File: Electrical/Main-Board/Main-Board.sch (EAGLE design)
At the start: 30 parts, among them IC1 ATMEGA16A-PU, IC2 ATMEGA16A-PU, IC3 TLE4966L, IC5 LM2904DRG3, IC6 TLE4966L, J1 FTSH-105-01-L-DV-K-A-P-TR, J2 0022288033, J3 0022288033, J4 PJ-031DH

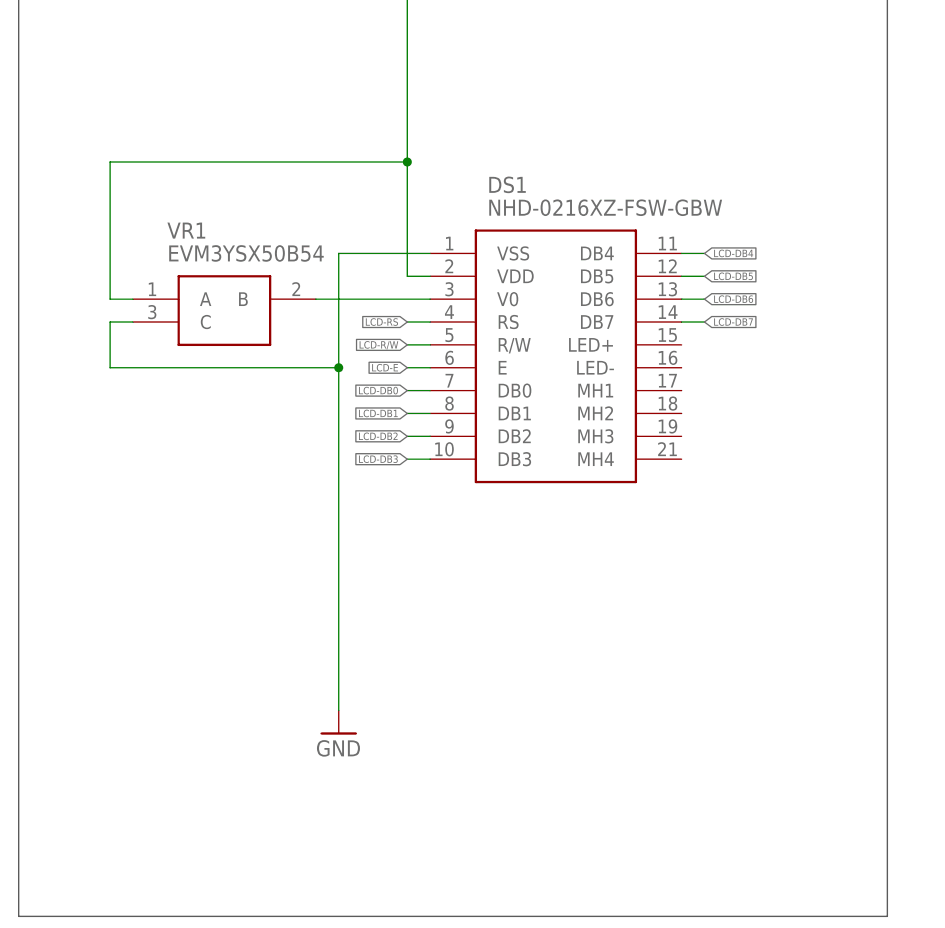
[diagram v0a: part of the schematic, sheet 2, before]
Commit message: Updated display footprint and fixed layout to suit it.
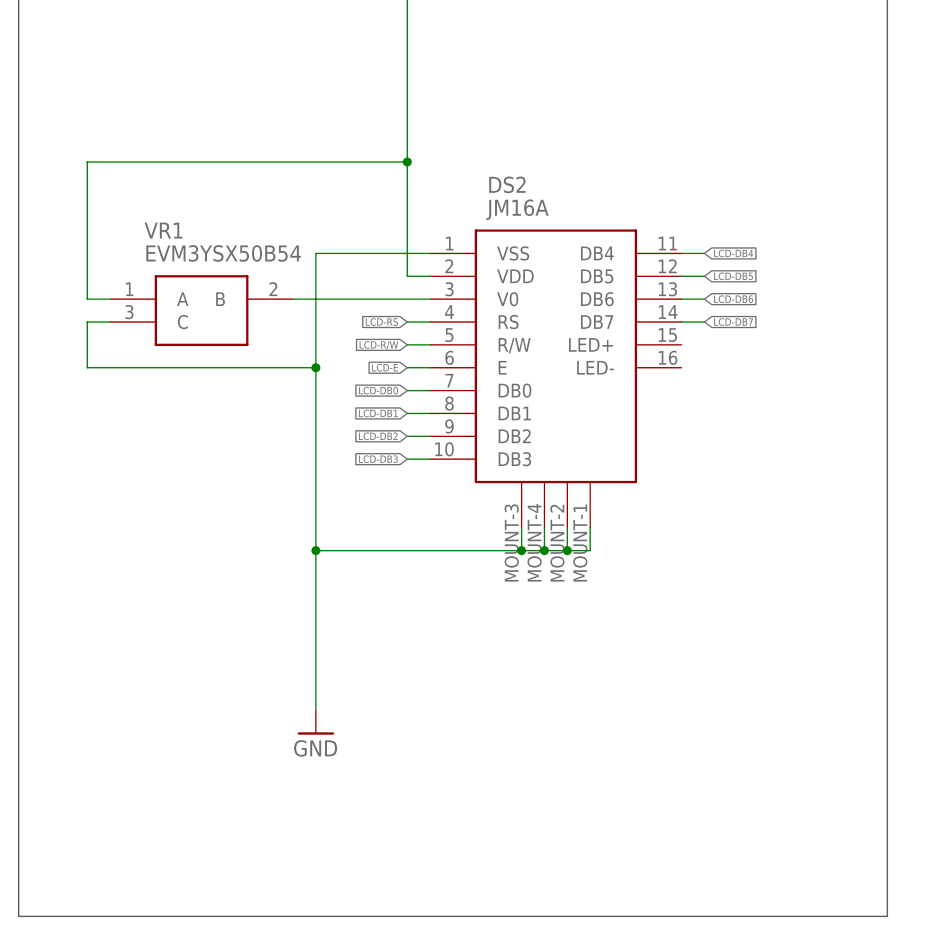
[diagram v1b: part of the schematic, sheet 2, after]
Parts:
- removed DS1: NHD-0216XZ-FSW-GBW, SamacSys_Parts:NHD-0216XZ-FSW-GBW
- added DS2: JM16A, JM16A-Vanheden:JM16A
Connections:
- net +5V/1: now also DS2.VDD; no longer DS1.VDD
- net GND: now also DS2.MOUNT-1, DS2.MOUNT-2, DS2.MOUNT-3, DS2.MOUNT-4, DS2.VSS; no longer DS1.VSS
- net LCD-DB0: now also DS2.DB0; no longer DS1.DB0
- net LCD-DB1: now also DS2.DB1; no longer DS1.DB1
- net LCD-DB2: now also DS2.DB2; no longer DS1.DB2
- net LCD-DB3: now also DS2.DB3; no longer DS1.DB3
- net LCD-DB4: now also DS2.DB4; no longer DS1.DB4
- net LCD-DB5: now also DS2.DB5; no longer DS1.DB5
- net LCD-DB6: now also DS2.DB6; no longer DS1.DB6
- net LCD-DB7: now also DS2.DB7; no longer DS1.DB7
- net LCD-E: now also DS2.E; no longer DS1.E
- net LCD-R/W: now also DS2.R/W; no longer DS1.R/W
- net LCD-RS: now also DS2.RS; no longer DS1.RS
- net N$2: now also DS2.V0; no longer DS1.V0
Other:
- moved on the sheet: VR1
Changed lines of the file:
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@@
 <drawing>
 <settings>
-<setting alwaysvectorfont="no"/>
+<setting alwaysvectorfont="yes"/>
 <setting verticaltext="up"/>
 </settings>
@@
 <part name="S2" library="SamacSys_Parts" deviceset="PTS647SM50SMTR2LFS" device=""/>
 <part name="R4" library="rcl" library_urn="urn:adsk.eagle:library:334" deviceset="R-EU_" device="R0603" package3d_urn="urn:adsk.eagle:package:23555/3" value="10K/10%"/>
-<part name="DS1" library="SamacSys_Parts" deviceset="NHD-0216XZ-FSW-GBW" device=""/>
 <part name="GND6" library="supply1" library_urn="urn:adsk.eagle:library:371" deviceset="GND" device=""/>
 <part name="SUPPLY6" library="supply2" library_urn="urn:adsk.eagle:library:372" deviceset="+5V/1" device=""/>
@@
 <part name="FRAME3" library="frames" library_urn="urn:adsk.eagle:library:229" deviceset="A4L-LOC" device=""/>
 <part name="C7" library="SamacSys_Parts" deviceset="EEEFK1J220P" device=""/>
+<part name="DS2" library="JM16A-Vanheden" deviceset="JM16A" device=""/>
 </parts>
 <sheets>
@@
 <attribute name="SHEET" x="230.505" y="5.08" size="2.54" layer="94"/>
 </instance>
-<instance part="DS1" gate="G$1" x="66.04" y="104.14" smashed="yes">
-<attribute name="NAME" x="72.39" y="111.76" size="1.778" layer="95" align="center-left"/>
-<attribute name="VALUE" x="72.39" y="109.22" size="1.778" layer="96" align="center-left"/>
-</instance>
-<instance part="GND6" gate="1" x="55.88" y="50.8" smashed="yes">
-<attribute name="VALUE" x="53.34" y="48.26" size="1.778" layer="96"/>
+<instance part="GND6" gate="1" x="53.34" y="50.8" smashed="yes">
+<attribute name="VALUE" x="50.8" y="48.26" size="1.778" layer="96"/>
 </instance>
 <instance part="SUPPLY6" gate="G$1" x="63.5" y="137.16" smashed="yes">
 <attribute name="VALUE" x="60.325" y="140.335" size="1.778" layer="96"/>
 </instance>
-<instance part="VR1" gate="G$1" x="33.02" y="99.06" smashed="yes">
-<attribute name="NAME" x="36.83" y="106.68" size="1.778" layer="95" align="center-left"/>
-<attribute name="VALUE" x="36.83" y="104.14" size="1.778" layer="96" align="center-left"/>
+<instance part="VR1" gate="G$1" x="30.48" y="99.06" smashed="yes">
+<attribute name="NAME" x="34.29" y="106.68" size="1.778" layer="95" align="center-left"/>
+<attribute name="VALUE" x="34.29" y="104.14" size="1.778" layer="96" align="center-left"/>
 </instance>
 <instance part="JP1" gate="A" x="187.96" y="91.44" smashed="yes" rot="R180">
@@
 <instance part="SUPPLY9" gate="G$1" x="205.74" y="111.76" smashed="yes">
 <attribute name="VALUE" x="202.565" y="114.935" size="1.778" layer="96"/>
+</instance>
+<instance part="DS2" gate="G$1" x="66.04" y="104.14" smashed="yes">
+<attribute name="NAME" x="72.39" y="111.76" size="1.778" layer="95" align="center-left"/>
+<attribute name="VALUE" x="72.39" y="109.22" size="1.778" layer="96" align="center-left"/>
 </instance>
 </instances>
@@
 <net name="GND" class="0">
 <segment>
-<pinref part="DS1" gate="G$1" pin="VSS"/>
-<wire x1="66.04" y1="104.14" x2="55.88" y2="104.14" width="0.1524" layer="91"/>
-<wire x1="55.88" y1="104.14" x2="55.88" y2="91.44" width="0.1524" layer="91"/>
+<wire x1="66.04" y1="104.14" x2="53.34" y2="104.14" width="0.1524" layer="91"/>
+<wire x1="53.34" y1="104.14" x2="53.34" y2="91.44" width="0.1524" layer="91"/>
 <pinref part="GND6" gate="1" pin="GND"/>
 <pinref part="VR1" gate="G$1" pin="C"/>
-<wire x1="55.88" y1="91.44" x2="55.88" y2="53.34" width="0.1524" layer="91"/>
-<wire x1="33.02" y1="96.52" x2="30.48" y2="96.52" width="0.1524" layer="91"/>
-<wire x1="30.48" y1="96.52" x2="30.48" y2="91.44" width="0.1524" layer="91"/>
-<wire x1="30.48" y1="91.44" x2="55.88" y2="91.44" width="0.1524" layer="91"/>
-<junction x="55.88" y="91.44"/>
+<wire x1="53.34" y1="91.44" x2="53.34" y2="71.12" width="0.1524" layer="91"/>
+<wire x1="53.34" y1="71.12" x2="53.34" y2="53.34" width="0.1524" layer="91"/>
+<wire x1="30.48" y1="96.52" x2="27.94" y2="96.52" width="0.1524" layer="91"/>
+<wire x1="27.94" y1="96.52" x2="27.94" y2="91.44" width="0.1524" layer="91"/>
+<wire x1="27.94" y1="91.44" x2="53.34" y2="91.44" width="0.1524" layer="91"/>
+<junction x="53.34" y="91.44"/>
+<pinref part="DS2" gate="G$1" pin="VSS"/>
+<pinref part="DS2" gate="G$1" pin="MOUNT-1"/>
+<wire x1="76.2" y1="73.66" x2="76.2" y2="71.12" width="0.1524" layer="91"/>
+<wire x1="76.2" y1="71.12" x2="78.74" y2="71.12" width="0.1524" layer="91"/>
+<pinref part="DS2" gate="G$1" pin="MOUNT-2"/>
+<wire x1="78.74" y1="71.12" x2="78.74" y2="73.66" width="0.1524" layer="91"/>
+<wire x1="78.74" y1="71.12" x2="81.28" y2="71.12" width="0.1524" layer="91"/>
+<junction x="78.74" y="71.12"/>
+<pinref part="DS2" gate="G$1" pin="MOUNT-3"/>
+<wire x1="81.28" y1="71.12" x2="81.28" y2="73.66" width="0.1524" layer="91"/>
+<wire x1="81.28" y1="71.12" x2="83.82" y2="71.12" width="0.1524" layer="91"/>
+<junction x="81.28" y="71.12"/>
+<pinref part="DS2" gate="G$1" pin="MOUNT-4"/>
+<wire x1="83.82" y1="71.12" x2="83.82" y2="73.66" width="0.1524" layer="91"/>
+<wire x1="76.2" y1="71.12" x2="53.34" y2="71.12" width="0.1524" layer="91"/>
+<junction x="76.2" y="71.12"/>
+<junction x="53.34" y="71.12"/>
 </segment>
 <segment>
@@
 <net name="+5V/1" class="0">
 <segment>
-<pinref part="DS1" gate="G$1" pin="VDD"/>
 <wire x1="66.04" y1="101.6" x2="63.5" y2="101.6" width="0.1524" layer="91"/>
 <pinref part="SUPPLY6" gate="G$1" pin="+5V/1"/>
@@
 <pinref part="VR1" gate="G$1" pin="A"/>
 <wire x1="63.5" y1="114.3" x2="63.5" y2="134.62" width="0.1524" layer="91"/>
-<wire x1="33.02" y1="99.06" x2="30.48" y2="99.06" width="0.1524" layer="91"/>
-<wire x1="30.48" y1="99.06" x2="30.48" y2="114.3" width="0.1524" layer="91"/>
-<wire x1="30.48" y1="114.3" x2="63.5" y2="114.3" width="0.1524" layer="91"/>
+<wire x1="30.48" y1="99.06" x2="27.94" y2="99.06" width="0.1524" layer="91"/>
+<wire x1="27.94" y1="99.06" x2="27.94" y2="114.3" width="0.1524" layer="91"/>
+<wire x1="27.94" y1="114.3" x2="63.5" y2="114.3" width="0.1524" layer="91"/>
 <junction x="63.5" y="114.3"/>
+<pinref part="DS2" gate="G$1" pin="VDD"/>
 </segment>
 <segment>
@@
 <net name="LCD-DB0" class="0">
 <segment>
-<pinref part="DS1" gate="G$1" pin="DB0"/>
 <wire x1="66.04" y1="88.9" x2="63.5" y2="88.9" width="0.1524" layer="91"/>
 <label x="63.5" y="88.9" size="0.8128" layer="95" rot="R180" xref="yes"/>
+<pinref part="DS2" gate="G$1" pin="DB0"/>
 </segment>
 </net>
 <net name="LCD-DB1" class="0">
 <segment>
-<pinref part="DS1" gate="G$1" pin="DB1"/>
 <wire x1="66.04" y1="86.36" x2="63.5" y2="86.36" width="0.1524" layer="91"/>
 <label x="63.5" y="86.36" size="0.8128" layer="95" rot="R180" xref="yes"/>
+<pinref part="DS2" gate="G$1" pin="DB1"/>
 </segment>
 </net>
 <net name="LCD-DB2" class="0">
 <segment>
-<pinref part="DS1" gate="G$1" pin="DB2"/>
 <wire x1="66.04" y1="83.82" x2="63.5" y2="83.82" width="0.1524" layer="91"/>
 <label x="63.5" y="83.82" size="0.8128" layer="95" rot="R180" xref="yes"/>
+<pinref part="DS2" gate="G$1" pin="DB2"/>
 </segment>
 </net>
 <net name="LCD-DB3" class="0">
 <segment>
-<pinref part="DS1" gate="G$1" pin="DB3"/>
 <wire x1="66.04" y1="81.28" x2="63.5" y2="81.28" width="0.1524" layer="91"/>
 <label x="63.5" y="81.28" size="0.8128" layer="95" rot="R180" xref="yes"/>
+<pinref part="DS2" gate="G$1" pin="DB3"/>
 </segment>
 </net>
 <net name="LCD-DB4" class="0">
 <segment>
-<pinref part="DS1" gate="G$1" pin="DB4"/>
 <wire x1="93.98" y1="104.14" x2="96.52" y2="104.14" width="0.1524" layer="91"/>
 <label x="96.52" y="104.14" size="0.8128" layer="95" xref="yes"/>
+<pinref part="DS2" gate="G$1" pin="DB4"/>
 </segment>
 </net>
 <net name="LCD-DB5" class="0">
 <segment>
-<pinref part="DS1" gate="G$1" pin="DB5"/>
 <wire x1="93.98" y1="101.6" x2="96.52" y2="101.6" width="0.1524" layer="91"/>
 <label x="96.52" y="101.6" size="0.8128" layer="95" xref="yes"/>
+<pinref part="DS2" gate="G$1" pin="DB5"/>
 </segment>
 </net>
 <net name="LCD-DB6" class="0">
 <segment>
-<pinref part="DS1" gate="G$1" pin="DB6"/>
 <wire x1="93.98" y1="99.06" x2="96.52" y2="99.06" width="0.1524" layer="91"/>
 <label x="96.52" y="99.06" size="0.8128" layer="95" xref="yes"/>
+<pinref part="DS2" gate="G$1" pin="DB6"/>
 </segment>
 </net>
 <net name="LCD-DB7" class="0">
 <segment>
-<pinref part="DS1" gate="G$1" pin="DB7"/>
 <wire x1="93.98" y1="96.52" x2="96.52" y2="96.52" width="0.1524" layer="91"/>
 <label x="96.52" y="96.52" size="0.8128" layer="95" xref="yes"/>
+<pinref part="DS2" gate="G$1" pin="DB7"/>
 </segment>
 </net>
 <net name="LCD-RS" class="0">
 <segment>
-<pinref part="DS1" gate="G$1" pin="RS"/>
 <wire x1="66.04" y1="96.52" x2="63.5" y2="96.52" width="0.1524" layer="91"/>
 <label x="63.5" y="96.52" size="0.8128" layer="95" rot="R180" xref="yes"/>
+<pinref part="DS2" gate="G$1" pin="RS"/>
 </segment>
 </net>
 <net name="LCD-R/W" class="0">
 <segment>
-<pinref part="DS1" gate="G$1" pin="R/W"/>
 <wire x1="66.04" y1="93.98" x2="63.5" y2="93.98" width="0.1524" layer="91"/>
 <label x="63.5" y="93.98" size="0.8128" layer="95" rot="R180" xref="yes"/>
+<pinref part="DS2" gate="G$1" pin="R/W"/>
 </segment>
 </net>
 <net name="LCD-E" class="0">
 <segment>
-<pinref part="DS1" gate="G$1" pin="E"/>
 <wire x1="66.04" y1="91.44" x2="63.5" y2="91.44" width="0.1524" layer="91"/>
 <label x="63.5" y="91.44" size="0.8128" layer="95" rot="R180" xref="yes"/>
+<pinref part="DS2" gate="G$1" pin="E"/>
 </segment>
 </net>
 <net name="N$2" class="0">
 <segment>
-<pinref part="DS1" gate="G$1" pin="V0"/>
 <pinref part="VR1" gate="G$1" pin="B"/>
-<wire x1="66.04" y1="99.06" x2="53.34" y2="99.06" width="0.1524" layer="91"/>
-</segment>
-</net>
+<wire x1="66.04" y1="99.06" x2="50.8" y2="99.06" width="0.1524" layer="91"/>
+<pinref part="DS2" gate="G$1" pin="V0"/>
+</segment>
+</net>

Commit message: Final PCB. Added GERBER files for MF
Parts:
- added JP2: (no value), pinhead:PINHD-1X2
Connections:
- new net N$3: IC2.[T1]_PB1, JP2.2
- net GND: now also JP2.1
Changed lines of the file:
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@@
 <part name="C7" library="SamacSys_Parts" deviceset="EEEFK1J220P" device=""/>
 <part name="DS2" library="JM16A-Vanheden" deviceset="JM16A" device=""/>
+<part name="JP2" library="pinhead" library_urn="urn:adsk.eagle:library:325" deviceset="PINHD-1X2" device="" package3d_urn="urn:adsk.eagle:package:22435/2"/>
+<part name="GND15" library="supply1" library_urn="urn:adsk.eagle:library:371" deviceset="GND" device=""/>
 </parts>
 <sheets>
@@
 <attribute name="VALUE" x="72.39" y="125.73" size="1.778" layer="96" align="center-left"/>
 </instance>
+<instance part="JP2" gate="G$1" x="284.48" y="180.34" smashed="yes" rot="R180">
+<attribute name="NAME" x="290.83" y="174.625" size="1.778" layer="95" rot="R180"/>
+<attribute name="VALUE" x="290.83" y="185.42" size="1.778" layer="96" rot="R180"/>
+</instance>
+<instance part="GND15" gate="1" x="292.1" y="167.64" smashed="yes">
+<attribute name="VALUE" x="289.56" y="165.1" size="1.778" layer="96"/>
+</instance>
 </instances>
 <busses>
@@
 <junction x="172.72" y="35.56"/>
 </segment>
+<segment>
+<pinref part="JP2" gate="G$1" pin="1"/>
+<wire x1="287.02" y1="177.8" x2="292.1" y2="177.8" width="0.1524" layer="91"/>
+<wire x1="292.1" y1="177.8" x2="292.1" y2="170.18" width="0.1524" layer="91"/>
+<pinref part="GND15" gate="1" pin="GND"/>
+</segment>
 </net>
 <net name="+5V/1" class="0">
@@
 </segment>
 </net>
+<net name="N$3" class="0">
+<segment>
+<pinref part="IC2" gate="G$1" pin="[T1]_PB1"/>
+<pinref part="JP2" gate="G$1" pin="2"/>
+<wire x1="297.18" y1="180.34" x2="287.02" y2="180.34" width="0.1524" layer="91"/>
+</segment>
+</net>
